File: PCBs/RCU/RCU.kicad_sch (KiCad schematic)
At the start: 0 parts

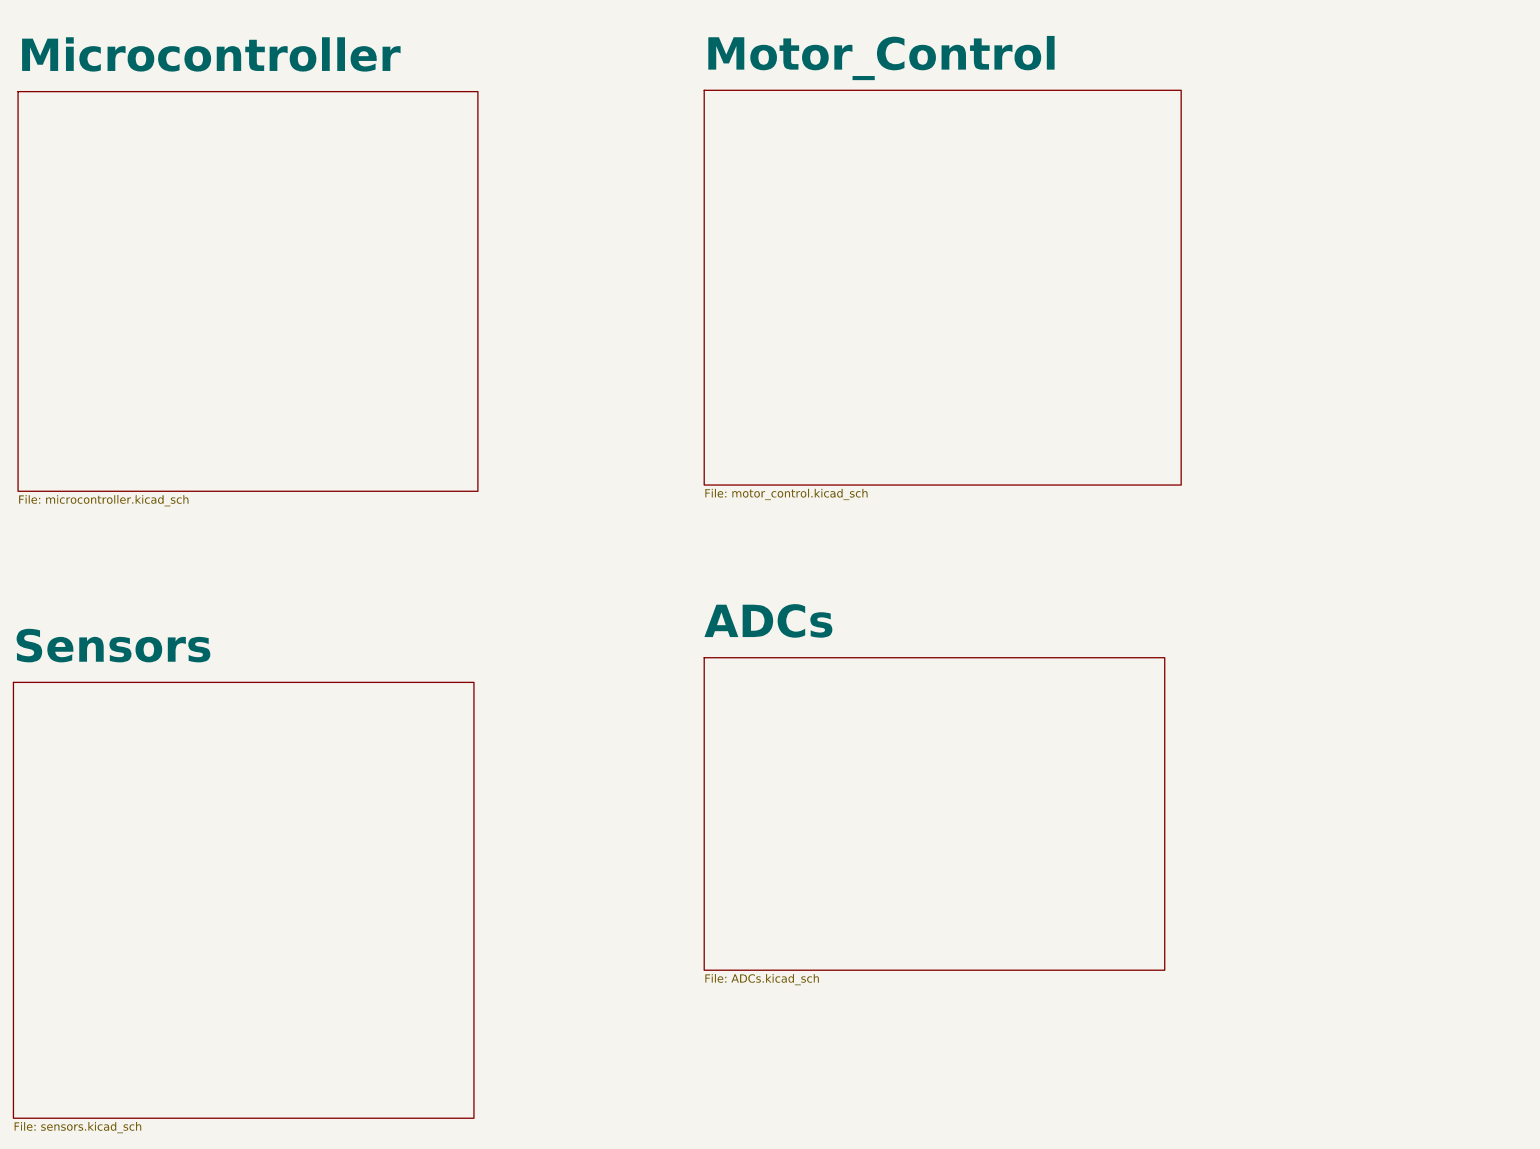
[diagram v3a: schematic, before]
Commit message: Added Bluetooth module ESP32-MINI-1
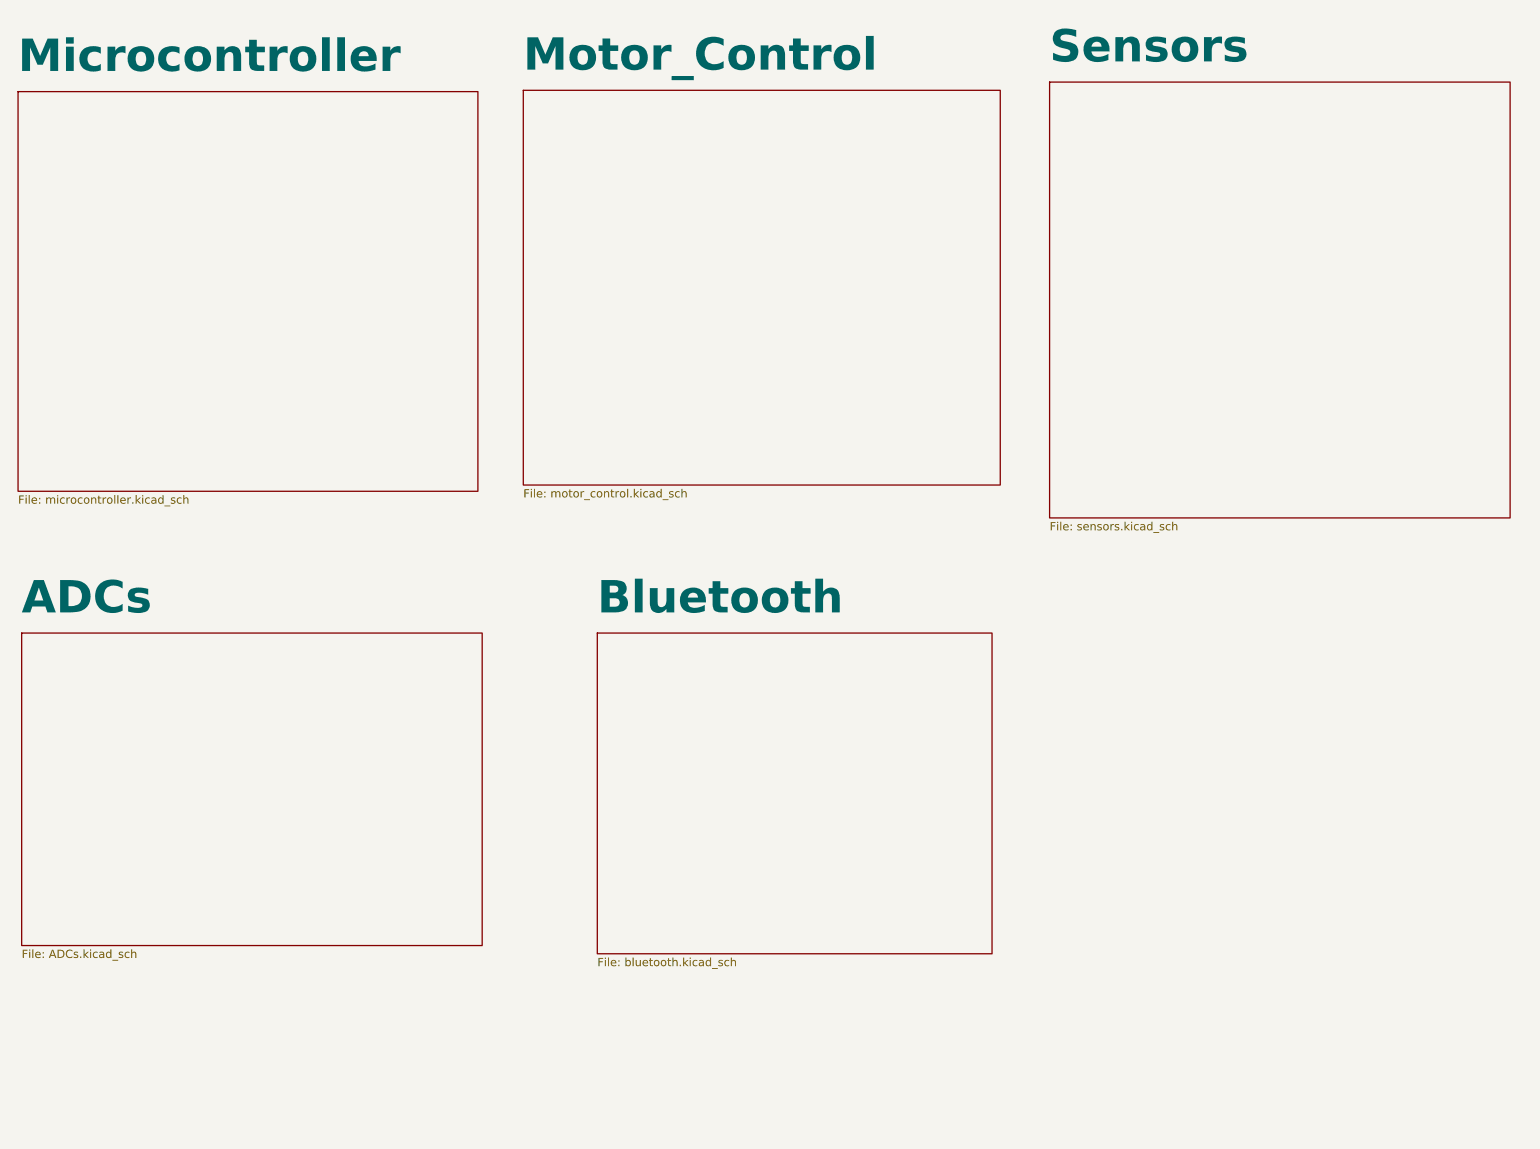
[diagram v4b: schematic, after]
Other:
- added sheet Bluetooth (bluetooth.kicad_sch)
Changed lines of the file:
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@@
 (kicad_sch (version 20211123) (generator eeschema)
   (paper "A4")
-  (sheet (at 139.7 26.67) (size 73.66 60.96) (fields_autoplaced)
-    (stroke (width 0.1524) (type solid) (color 0 0 0 0))
-    (fill (color 0 0 0 0.0000))
-    (property "Sheet name" "Motor_Control" (id 0) (at 139.7 24.0934 0)
-      (effects (font (size 5 5) bold) (justify left bottom))
-    )
-    (property "Sheet file" "motor_control.kicad_sch" (id 1) (at 139.7 88.2146 0)
-      (effects (font (size 1.27 1.27)) (justify left top))
-    )
-  )
-  (sheet (at 33.02 118.11) (size 71.12 67.31) (fields_autoplaced)
-    (stroke (width 0.1524) (type solid) (color 0 0 0 0))
-    (fill (color 0 0 0 0.0000))
-    (property "Sheet name" "Sensors" (id 0) (at 33.02 115.5334 0)
-      (effects (font (size 5 5) bold) (justify left bottom))
-    )
-    (property "Sheet file" "sensors.kicad_sch" (id 1) (at 33.02 186.0046 0)
+  (sheet (at 111.76 26.67) (size 73.66 60.96) (fields_autoplaced)
+    (stroke (width 0.1524) (type solid) (color 0 0 0 0))
+    (fill (color 0 0 0 0.0000))
+    (property "Sheet name" "Motor_Control" (id 0) (at 111.76 24.0934 0)
+      (effects (font (size 5 5) bold) (justify left bottom))
+    )
+    (property "Sheet file" "motor_control.kicad_sch" (id 1) (at 111.76 88.2146 0)
+      (effects (font (size 1.27 1.27)) (justify left top))
+    )
+  )
+  (sheet (at 123.19 110.49) (size 60.96 49.53) (fields_autoplaced)
+    (stroke (width 0.1524) (type solid) (color 0 0 0 0))
+    (fill (color 0 0 0 0.0000))
+    (property "Sheet name" "Bluetooth" (id 0) (at 123.19 107.9134 0)
+      (effects (font (size 5 5) bold) (justify left bottom))
+    )
+    (property "Sheet file" "bluetooth.kicad_sch" (id 1) (at 123.19 160.6046 0)
+      (effects (font (size 1.27 1.27)) (justify left top))
+    )
+  )
+  (sheet (at 193.04 25.4) (size 71.12 67.31) (fields_autoplaced)
+    (stroke (width 0.1524) (type solid) (color 0 0 0 0))
+    (fill (color 0 0 0 0.0000))
+    (property "Sheet name" "Sensors" (id 0) (at 193.04 22.8234 0)
+      (effects (font (size 5 5) bold) (justify left bottom))
+    )
+    (property "Sheet file" "sensors.kicad_sch" (id 1) (at 193.04 93.2946 0)
       (effects (font (size 1.27 1.27)) (justify left top))
     )
@@
     )
   )
-  (sheet (at 139.7 114.3) (size 71.12 48.26) (fields_autoplaced)
-    (stroke (width 0.1524) (type solid) (color 0 0 0 0))
-    (fill (color 0 0 0 0.0000))
-    (property "Sheet name" "ADCs" (id 0) (at 139.7 111.7234 0)
-      (effects (font (size 5 5) bold) (justify left bottom))
-    )
-    (property "Sheet file" "ADCs.kicad_sch" (id 1) (at 139.7 163.1446 0)
+  (sheet (at 34.29 110.49) (size 71.12 48.26) (fields_autoplaced)
+    (stroke (width 0.1524) (type solid) (color 0 0 0 0))
+    (fill (color 0 0 0 0.0000))
+    (property "Sheet name" "ADCs" (id 0) (at 34.29 107.9134 0)
+      (effects (font (size 5 5) bold) (justify left bottom))
+    )
+    (property "Sheet file" "ADCs.kicad_sch" (id 1) (at 34.29 159.3346 0)
       (effects (font (size 1.27 1.27)) (justify left top))
     )
@@
     (path "/6678d44b-178f-4b7c-833f-18a4e680f820" (page "4"))
     (path "/d249f484-be7b-4fe1-aa74-bf5965c8a2c2" (page "5"))
+    (path "/2af55460-e33d-4dc0-b588-5a5fc90e3fb4" (page "6"))
   )
   (symbol_instances
@@
       (reference "#PWR?") (unit 1) (value "+3.3V") (footprint "")
     )
+    (path "/2af55460-e33d-4dc0-b588-5a5fc90e3fb4/890956a6-3f07-43bc-974d-ebd2244f048f"
+      (reference "#PWR?") (unit 1) (value "GND") (footprint "")
+    )
     (path "/c46a482e-bfa4-4ed5-a49f-3179709c39a1/8f435151-c909-4cdf-a7f9-67c1f7b1e16c"
       (reference "#PWR?") (unit 1) (value "GND") (footprint "")
@@
       (reference "#PWR?") (unit 1) (value "GND") (footprint "")
     )
+    (path "/2af55460-e33d-4dc0-b588-5a5fc90e3fb4/b87ed7b4-61ef-4f86-b3eb-1f4aab40dcdb"
+      (reference "#PWR?") (unit 1) (value "+3.3V") (footprint "")
+    )
     (path "/2537d888-fd78-4661-a6de-7d85959a9016/bc0f5d15-d5e7-48e9-a52f-8746301523de"
       (reference "#PWR?") (unit 1) (value "GND") (footprint "")
@@
     (path "/2537d888-fd78-4661-a6de-7d85959a9016/d83684cc-8cc6-4e75-ba87-39c1c6e5d2a2"
       (reference "#PWR?") (unit 1) (value "GND") (footprint "")
+    )
+    (path "/2af55460-e33d-4dc0-b588-5a5fc90e3fb4/e6783f94-afe7-4afe-bf64-528e13b691e6"
+      (reference "#PWR?") (unit 1) (value "+3.3V") (footprint "")
     )
     (path "/2537d888-fd78-4661-a6de-7d85959a9016/eb697269-33ec-4812-82a3-54942437b68e"
@@
       (reference "U?") (unit 1) (value "DRV8876") (footprint "")
     )
+    (path "/2af55460-e33d-4dc0-b588-5a5fc90e3fb4/bc18ee3a-4ef4-47ff-b72c-4578b85f91f7"
+      (reference "U?") (unit 1) (value "ESP32-MINI-1") (footprint "")
+    )
     (path "/6678d44b-178f-4b7c-833f-18a4e680f820/d7ca4669-23a4-4571-85ab-fbd03c4b29b9"

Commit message: Start drafting power module
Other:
- added sheet Power (Power.kicad_sch)
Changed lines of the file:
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@@
+    )
+  )
+  (sheet (at 196.85 109.22) (size 69.85 46.99) (fields_autoplaced)
+    (stroke (width 0.1524) (type solid) (color 0 0 0 0))
+    (fill (color 0 0 0 0.0000))
+    (property "Sheet name" "Power" (id 0) (at 196.85 106.6434 0)
+      (effects (font (size 5 5) bold) (justify left bottom))
+    )
+    (property "Sheet file" "Power.kicad_sch" (id 1) (at 196.85 156.7946 0)
+      (effects (font (size 1.27 1.27)) (justify left top))
     )
   )
@@
     (path "/d249f484-be7b-4fe1-aa74-bf5965c8a2c2" (page "5"))
     (path "/2af55460-e33d-4dc0-b588-5a5fc90e3fb4" (page "6"))
+    (path "/b265f195-de32-404f-a73c-b2d5ee499e9b" (page "7"))
   )
   (symbol_instances
@@
       (reference "U?") (unit 1) (value "DRV8876") (footprint "")
     )
+    (path "/b265f195-de32-404f-a73c-b2d5ee499e9b/251cc7e0-05f8-4ffb-916c-a28f1d284645"
+      (reference "U?") (unit 1) (value "AP63203WU") (footprint "Package_TO_SOT_SMD:TSOT-23-6")
+    )
     (path "/6678d44b-178f-4b7c-833f-18a4e680f820/455511d5-40a2-4651-ab9c-da84f8d67b49"
       (reference "U?") (unit 1) (value "SHT30-DIS") (footprint "Sensor_Humidity:Sensirion_DFN-8-1EP_2.5x2.5mm_P0.5mm_EP1.1x1.7mm")
     )
+    (path "/b265f195-de32-404f-a73c-b2d5ee499e9b/7c239421-0ca0-4d78-b32c-940aa174322b"
+      (reference "U?") (unit 1) (value "AZ1117-3.3") (footprint "")
+    )
     (path "/d249f484-be7b-4fe1-aa74-bf5965c8a2c2/7feb8a1b-3f2a-4be2-82b2-706f9df82096"
       (reference "U?") (unit 1) (value "MCP3021A5T-E/OT") (footprint "")
@@
       (reference "U?") (unit 1) (value "OPA365xxD") (footprint "Package_SO:SOIC-8_3.9x4.9mm_P1.27mm")
     )
+    (path "/b265f195-de32-404f-a73c-b2d5ee499e9b/a3770f69-657c-4417-b746-239881687437"
+      (reference "U?") (unit 1) (value "AP63203WU") (footprint "Package_TO_SOT_SMD:TSOT-23-6")
+    )
     (path "/2537d888-fd78-4661-a6de-7d85959a9016/a6943a68-4b84-4b97-bc31-8d22c0a001ae"
